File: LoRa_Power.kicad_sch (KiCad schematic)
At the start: 12 parts, among them U15 TPS7A4501DCQT, U16 ADM1176-1ARMZ-R7, U7 E22-900M30S

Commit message: temp
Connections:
- net LoRa_CSn is gone; now on net CSn: U7.19 (NSS)
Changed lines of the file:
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@@
+		)
+	)
+	(label "LoRa_CSn"
+		(at 243.84 123.19 0)
+		(fields_autoplaced yes)
+		(effects
+			(font
+				(size 1.27 1.27)
+			)
+			(justify left bottom)
 		)
 	)
@@
 	(label "CLK"
 		(at 243.84 127 0)
-		(fields_autoplaced yes)
-		(effects
-			(font
-				(size 1.27 1.27)
-			)
-			(justify left bottom)
-		)
-	)
-	(label "CSn"
-		(at 243.84 123.19 0)
 		(fields_autoplaced yes)
 		(effects
@@
 		)
 	)
-	(hierarchical_label "SDA_BUS"
+	(hierarchical_label "SDA"
 		(shape bidirectional)
 		(at 260.35 52.07 0)
@@
 		)
 	)
-	(hierarchical_label "SCL_BUS"
+	(hierarchical_label "SCL"
 		(shape bidirectional)
 		(at 260.35 49.53 0)

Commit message: v1 done
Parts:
- removed R53, R54: 10K, Resistor_SMD:R_0603_1608Metric, symbol Device:R_Small
- added R23, R24: 10K, Resistor_SMD:R_0603_1608Metric, symbol Device:R_Small
- U15: symbol Mainboard:TPS7A4501DCQT -> Argus-IC:TPS7A4501DCQT
- U16: symbol Mainboard:ADM1176-1ARMZ-R7 -> Argus-IC:ADM1176-1ARMZ-R7
- U7: symbol Mainboard:E22-900M30S -> Argus-Miscellaneous:E22-900M30S-SX1262
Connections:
- net GND: now also R23.2, R24.2
- net LoRa_RX_EN: now also R24.1
- net LoRa_TX_EN: now also R23.1

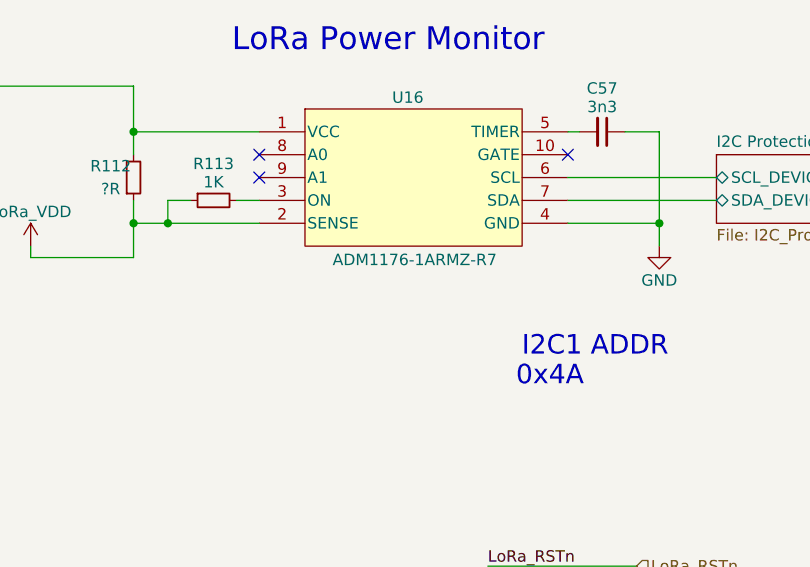
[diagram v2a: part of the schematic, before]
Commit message: Updated i2c device addresses and mcu caps
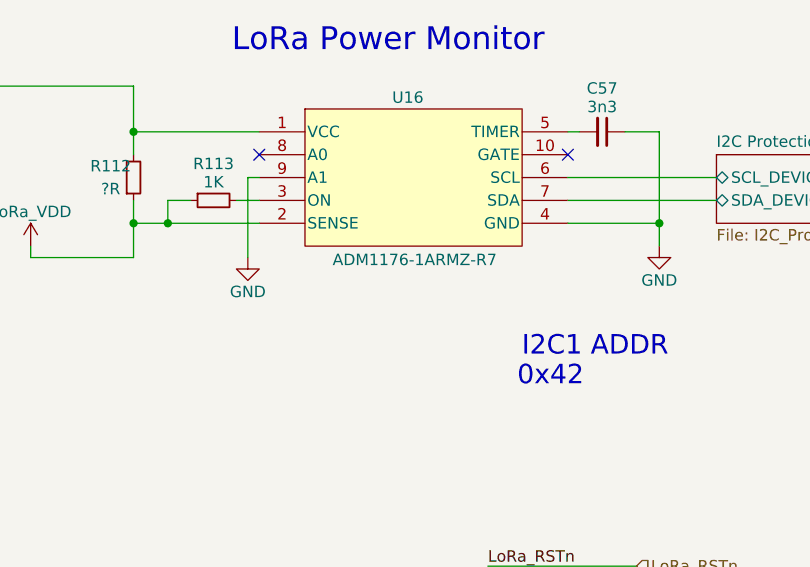
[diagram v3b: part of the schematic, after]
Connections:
- net GND: now also U16.9 (A1)
- no-connect marks 4 -> 3
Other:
- note added: "0x42"
- note removed: "0x4A"
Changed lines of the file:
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@@
 	)
 	(no_connect
-		(at 176.53 49.53)
+		(at 210.82 46.99)
 	)
 	(no_connect
 		(at 176.53 46.99)
 	)
-	(no_connect
-		(at 210.82 46.99)
-	)
 	(wire
 		(pts
@@
 	(wire
 		(pts
+			(xy 175.26 49.53) (xy 175.26 58.42)
+		)
+		(stroke
+			(width 0)
+			(type default)
+		)
+	)
+	(wire
+		(pts
 			(xy 39.37 143.51) (xy 39.37 140.97)
 		)
@@
 		(pts
 			(xy 106.68 52.07) (xy 106.68 59.69)
+		)
+		(stroke
+			(width 0)
+			(type default)
+		)
+	)
+	(wire
+		(pts
+			(xy 176.53 49.53) (xy 175.26 49.53)
 		)
 		(stroke
@@
 		)
 	)
-	(text "0x4A"
+	(text "0x42"
 		(exclude_from_sim no)
 		(at 212.598 72.898 0)
@@
 					(unit 1)
 				)
+			)
+		)
+	)
+	(symbol
+		(lib_id "power:GND")
+		(at 175.26 58.42 0)
+		(unit 1)
+		(exclude_from_sim no)
+		(in_bom yes)
+		(on_board yes)
+		(dnp no)
+		(property "Reference" "#PWR0154"
+			(at 175.26 64.77 0)
+			(effects
+				(font
+					(size 1.27 1.27)
+				)
+				(hide yes)
+			)
+		)
+		(property "Value" "GND"
+			(at 175.26 62.23 0)
+			(effects
+				(font
+					(size 1.27 1.27)
+				)
+			)
+		)
+		(property "Footprint" ""
+			(at 175.26 58.42 0)
+			(effects
+				(font
+					(size 1.27 1.27)
+				)
+				(hide yes)
+			)
+		)
+		(property "Datasheet" ""
+			(at 175.26 58.42 0)
+			(effects
+				(font
+					(size 1.27 1.27)
+				)
+				(hide yes)
+			)
+		)
+		(property "Description" "Power symbol creates a global label with name \"GND\" , ground"
+			(at 175.26 58.42 0)
+			(effects
+				(font
+					(size 1.27 1.27)
+				)
+				(hide yes)
+			)
+		)
+		(pin "1"
+		)
+		(instances
+			(project "Avionics-MainBoard"
+				(path "/4c932743-8c6f-426e-9c1f-5a3f2b32c70d/6167394f-ef17-4174-a137-33bfda5b3a14"
+					(reference "#PWR0154")
+					(unit 1)
+				)

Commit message: Added extra connector
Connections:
- net LoRa_DIO1: no longer U7.13 (DIO1)
- net LoRa_DIO2: no longer U7.8 (DIO2)
- no-connect marks 3 -> 5
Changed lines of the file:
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@@
+	)
+	(no_connect
+		(at 95.25 124.46)
 	)
 	(no_connect
@@
 		(at 176.53 46.99)
 	)
+	(no_connect
+		(at 60.96 134.62)
+	)
 	(wire
 		(pts
@@
 	(wire
 		(pts
-			(xy 95.25 124.46) (xy 110.49 124.46)
-		)
-		(stroke
-			(width 0)
-			(type default)
-		)
-	)
-	(wire
-		(pts
 			(xy 77.47 58.42) (xy 77.47 55.88)
 		)
@@
 		(pts
 			(xy 106.68 60.96) (xy 106.68 59.69)
-		)
-		(stroke
-			(width 0)
-			(type default)
-		)
-	)
-	(wire
-		(pts
-			(xy 49.53 134.62) (xy 60.96 134.62)
 		)
 		(stroke
@@
 		)
 	)
-	(label "LoRa_DIO1"
-		(at 99.06 124.46 0)
+	(label "LoRa_TX_EN"
+		(at 36.83 132.08 0)
 		(fields_autoplaced yes)
 		(effects
@@
 		)
 	)
-	(label "LoRa_TX_EN"
-		(at 36.83 132.08 0)
-		(fields_autoplaced yes)
-		(effects
-			(font
-				(size 1.27 1.27)
-			)
-			(justify left bottom)
-		)
-	)
 	(label "MISO"
 		(at 243.84 134.62 0)
 		(fields_autoplaced yes)
 		(effects
-			(font
-				(size 1.27 1.27)
-			)
-			(justify left bottom)
-		)
-	)
-	(label "LoRa_DIO2"
-		(at 49.53 134.62 0)
-		(fields_autoplaced yes)
-		(effects

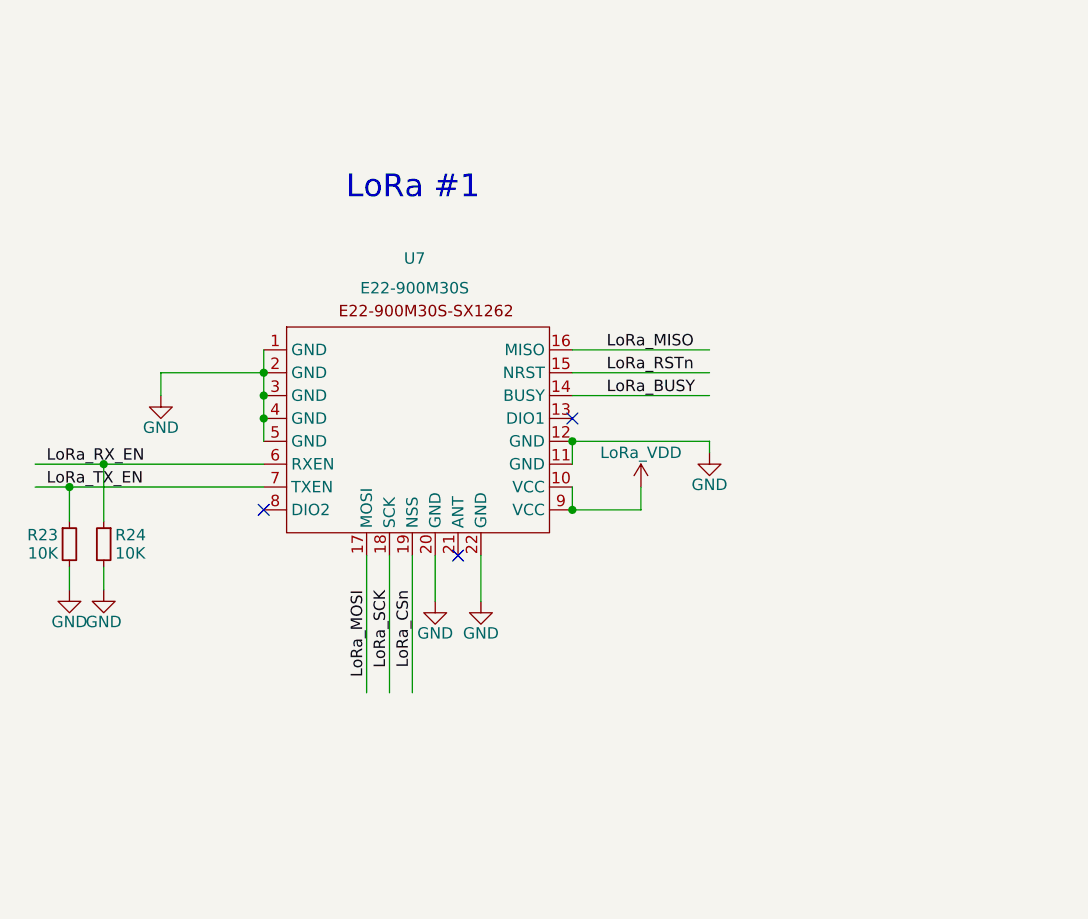
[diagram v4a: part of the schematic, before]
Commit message: Silkscreen hiding
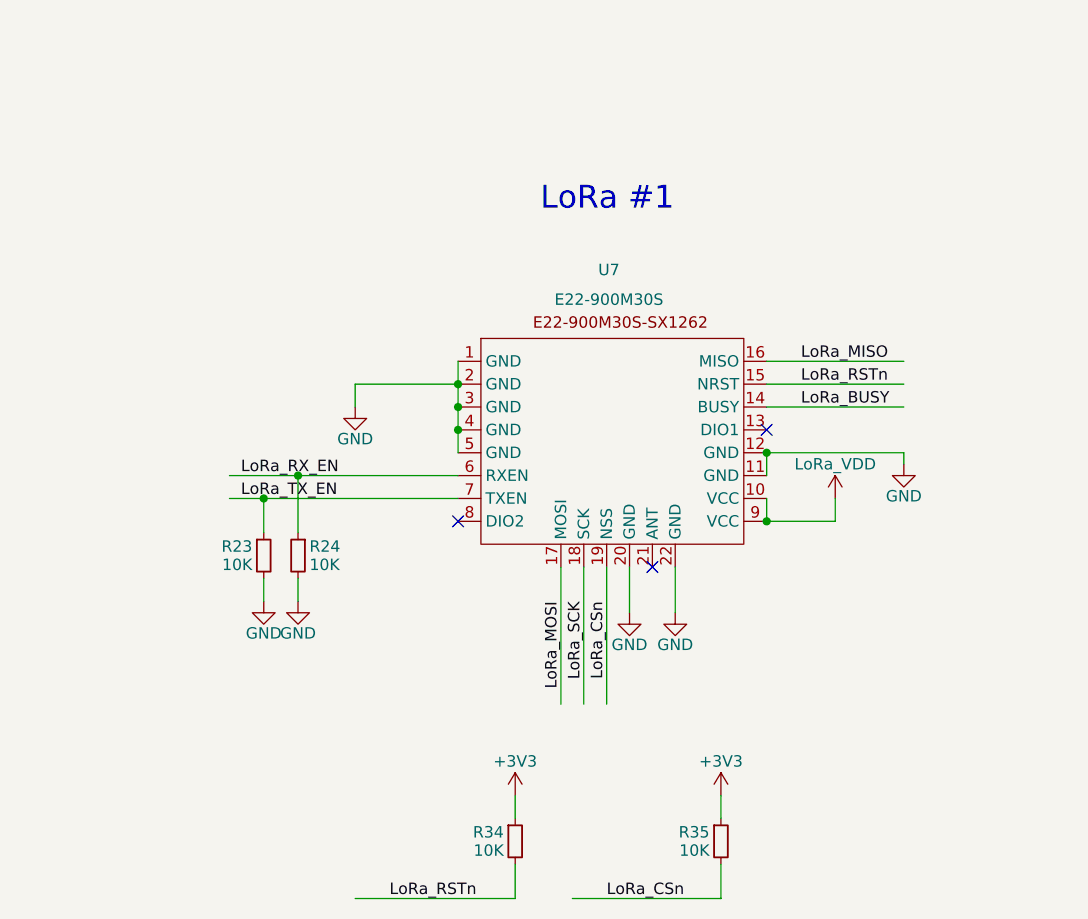
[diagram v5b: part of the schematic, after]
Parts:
- added R34, R35: 10K, Resistor_SMD:R_0603_1608Metric, symbol Device:R_Small
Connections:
- net CSn: now also R35.2
- net LoRa_RSTn: now also R34.2
- new net +3V3: R34.1, R35.1
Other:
- moved on the sheet: R23, R24, U7

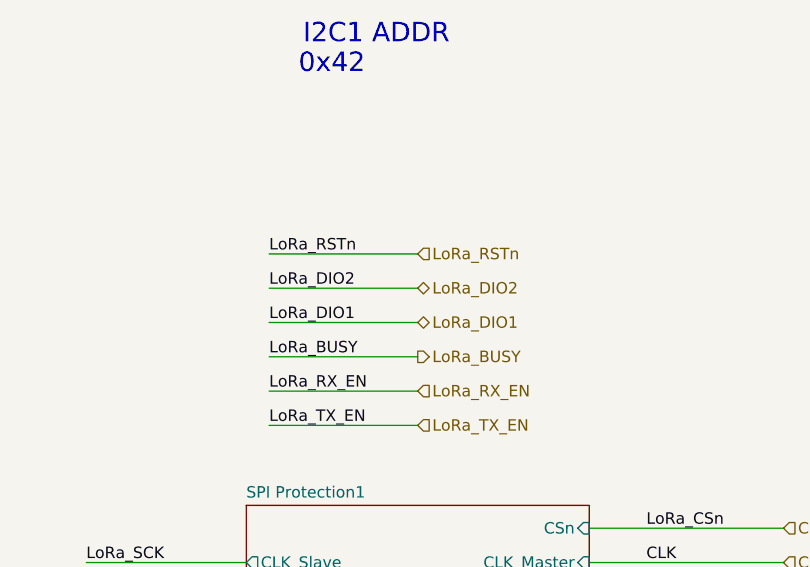
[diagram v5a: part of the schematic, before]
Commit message: Fixed schematic bugs and corresponding layout modifications
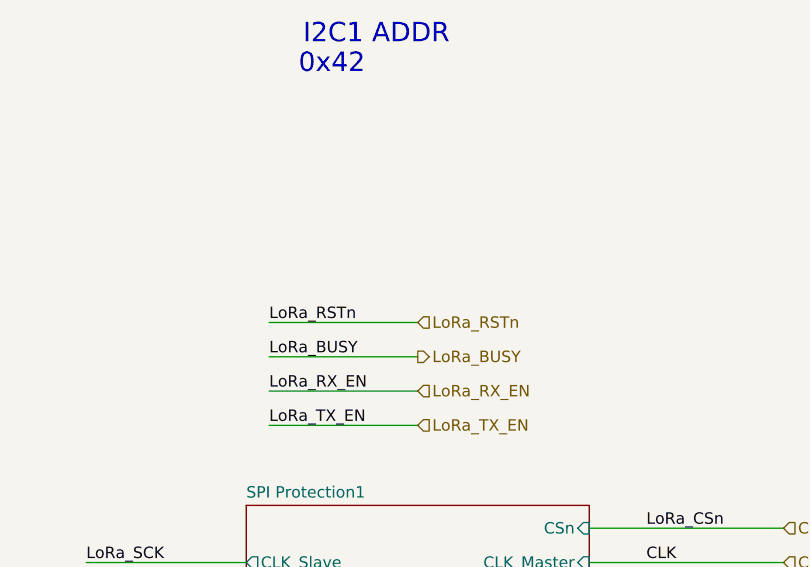
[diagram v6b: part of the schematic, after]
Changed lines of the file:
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@@
 	(wire
 		(pts
-			(xy 201.93 92.71) (xy 218.44 92.71)
+			(xy 201.93 100.33) (xy 218.44 100.33)
 		)
 		(stroke
@@
 	(wire
 		(pts
-			(xy 201.93 96.52) (xy 218.44 96.52)
-		)
-		(stroke
-			(width 0)
-			(type default)
-		)
-	)
-	(wire
-		(pts
 			(xy 111.76 173.99) (xy 111.76 177.8)
 		)
@@
 		(pts
 			(xy 82.55 123.19) (xy 82.55 125.73)
-		)
-		(stroke
-			(width 0)
-			(type default)
-		)
-	)
-	(wire
-		(pts
-			(xy 201.93 100.33) (xy 218.44 100.33)
 		)
 		(stroke
@@
 		)
 	)
-	(label "LoRa_DIO2"
-		(at 201.93 96.52 0)
-		(fields_autoplaced yes)
-		(effects
-			(font
-				(size 1.27 1.27)
-			)
-			(justify left bottom)
-		)
-	)
 	(label "LoRa_MOSI"
 		(at 181.61 130.81 0)
@@
 		)
 	)
-	(label "LoRa_DIO1"
-		(at 201.93 100.33 0)
-		(fields_autoplaced yes)
-		(effects
-			(font
-				(size 1.27 1.27)
-			)
-			(justify left bottom)
-		)
-	)
 	(label "LoRa_CSn"
 		(at 99.06 144.78 270)
@@
 	)
 	(label "LoRa_RSTn"
-		(at 201.93 92.71 0)
+		(at 201.93 100.33 0)
 		(fields_autoplaced yes)
 		(effects
@@
 			)
 			(justify left bottom)
-		)
-	)
-	(hierarchical_label "LoRa_DIO2"
-		(shape bidirectional)
-		(at 218.44 96.52 0)
-		(fields_autoplaced yes)
-		(effects
-			(font
-				(size 1.27 1.27)
-			)
-			(justify left)
 		)
 	)
@@
 	(hierarchical_label "LoRa_RSTn"
 		(shape input)
-		(at 218.44 92.71 0)
+		(at 218.44 100.33 0)
 		(fields_autoplaced yes)
 		(effects
@@
 		(fields_autoplaced yes)
 		(effects
-			(font
-				(size 1.27 1.27)
-			)
-			(justify left)
-		)
-	)
-	(hierarchical_label "LoRa_DIO1"
-		(shape bidirectional)
-		(at 218.44 100.33 0)
-		(fields_autoplaced yes)
-		(effects

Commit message: Minor fixes, export BOM
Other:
- moved on the sheet: C57
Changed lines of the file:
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@@
 	(wire
 		(pts
-			(xy 210.82 44.45) (xy 212.09 44.45)
+			(xy 210.82 44.45) (xy 213.36 44.45)
 		)
 		(stroke
@@
 	(wire
 		(pts
-			(xy 220.98 44.45) (xy 217.17 44.45)
+			(xy 220.98 44.45) (xy 218.44 44.45)
 		)
 		(stroke
@@
 		(dnp no)
 		(property "Reference" "R112"
-			(at 160.02 48.26 0)
+			(at 158.75 48.514 0)
 			(effects
 				(font
@@
 		)
 		(property "Value" "?R"
-			(at 160.02 50.8 0)
+			(at 160.02 50.546 0)
 			(effects
 				(font
@@
 	(symbol
 		(lib_id "Device:C_Small")
-		(at 214.63 44.45 270)
+		(at 215.9 44.45 270)
 		(unit 1)
 		(exclude_from_sim no)
@@
 		(dnp no)
 		(property "Reference" "C57"
-			(at 214.63 39.624 90)
+			(at 215.9 39.624 90)
 			(effects
 				(font
@@
 		)
 		(property "Value" "3n3"
-			(at 214.63 41.6814 90)
+			(at 215.9 41.6814 90)
 			(effects
 				(font
@@
 		)
 		(property "Footprint" "Capacitor_SMD:C_0603_1608Metric"
-			(at 214.63 44.45 0)
+			(at 215.9 44.45 0)
 			(effects
 				(font
@@
 		)
 		(property "Datasheet" ""
-			(at 214.63 44.45 0)
+			(at 215.9 44.45 0)
 			(effects
 				(font
@@
 		)
 		(property "Description" "3.3nF +-10% 100V X7R 0603"
-			(at 214.63 44.45 0)
-			(effects
-				(font
+			(at 215.9 44.45 0)
+			(effects
+				(font

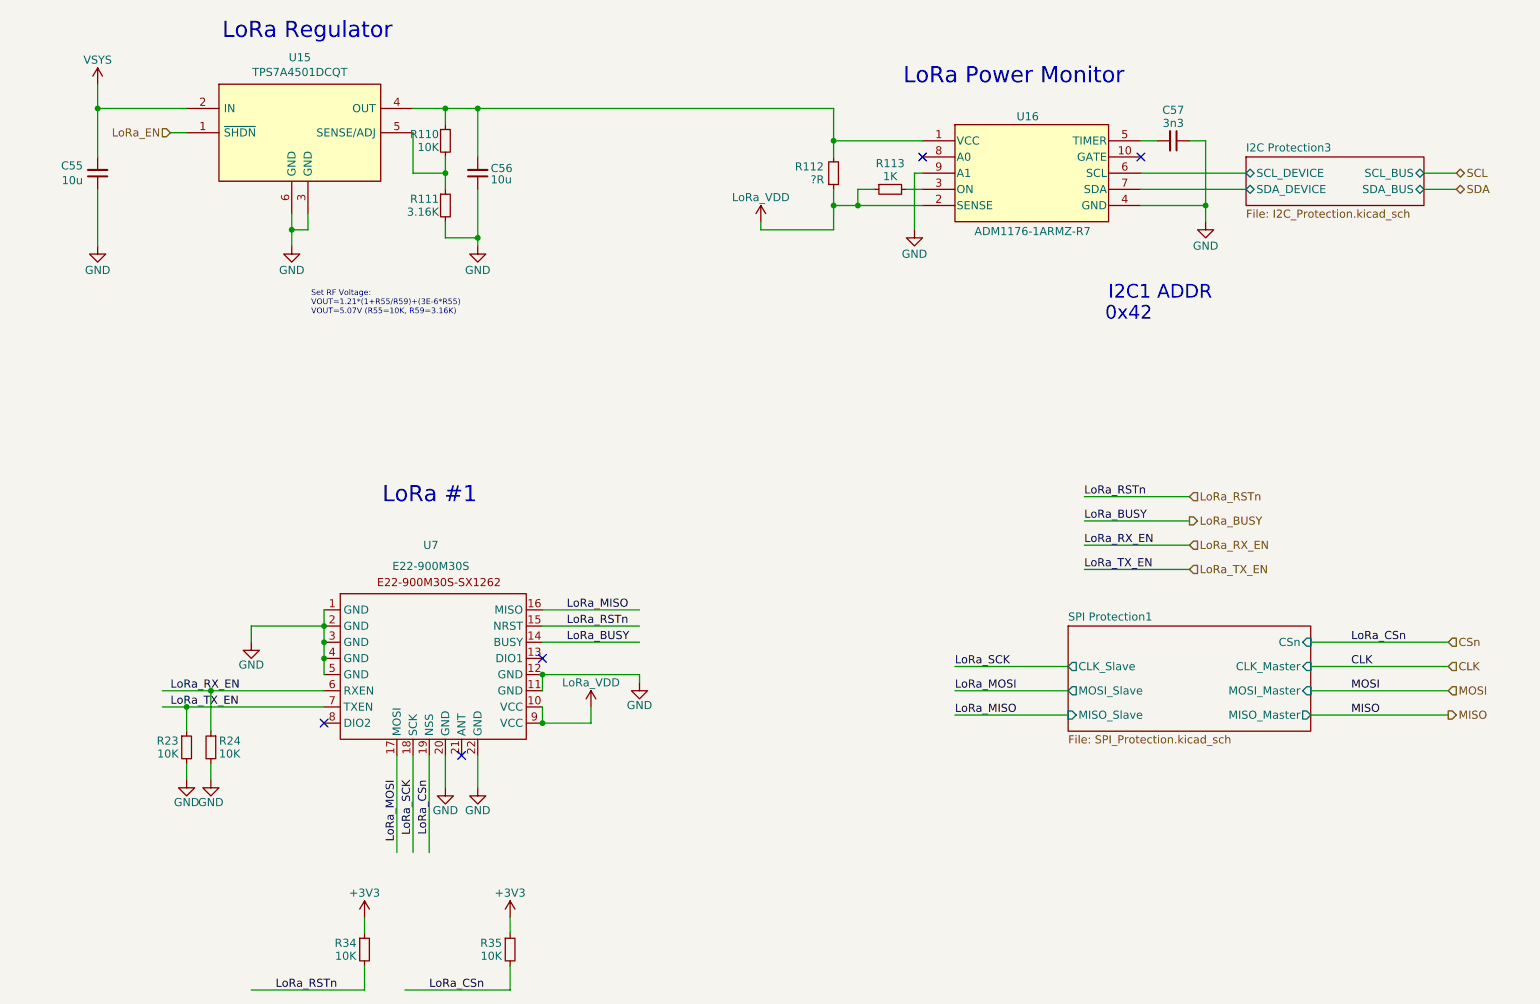
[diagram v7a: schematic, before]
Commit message: Added better protection to SD card, Jetson IO, and added address breakouts to power monitors
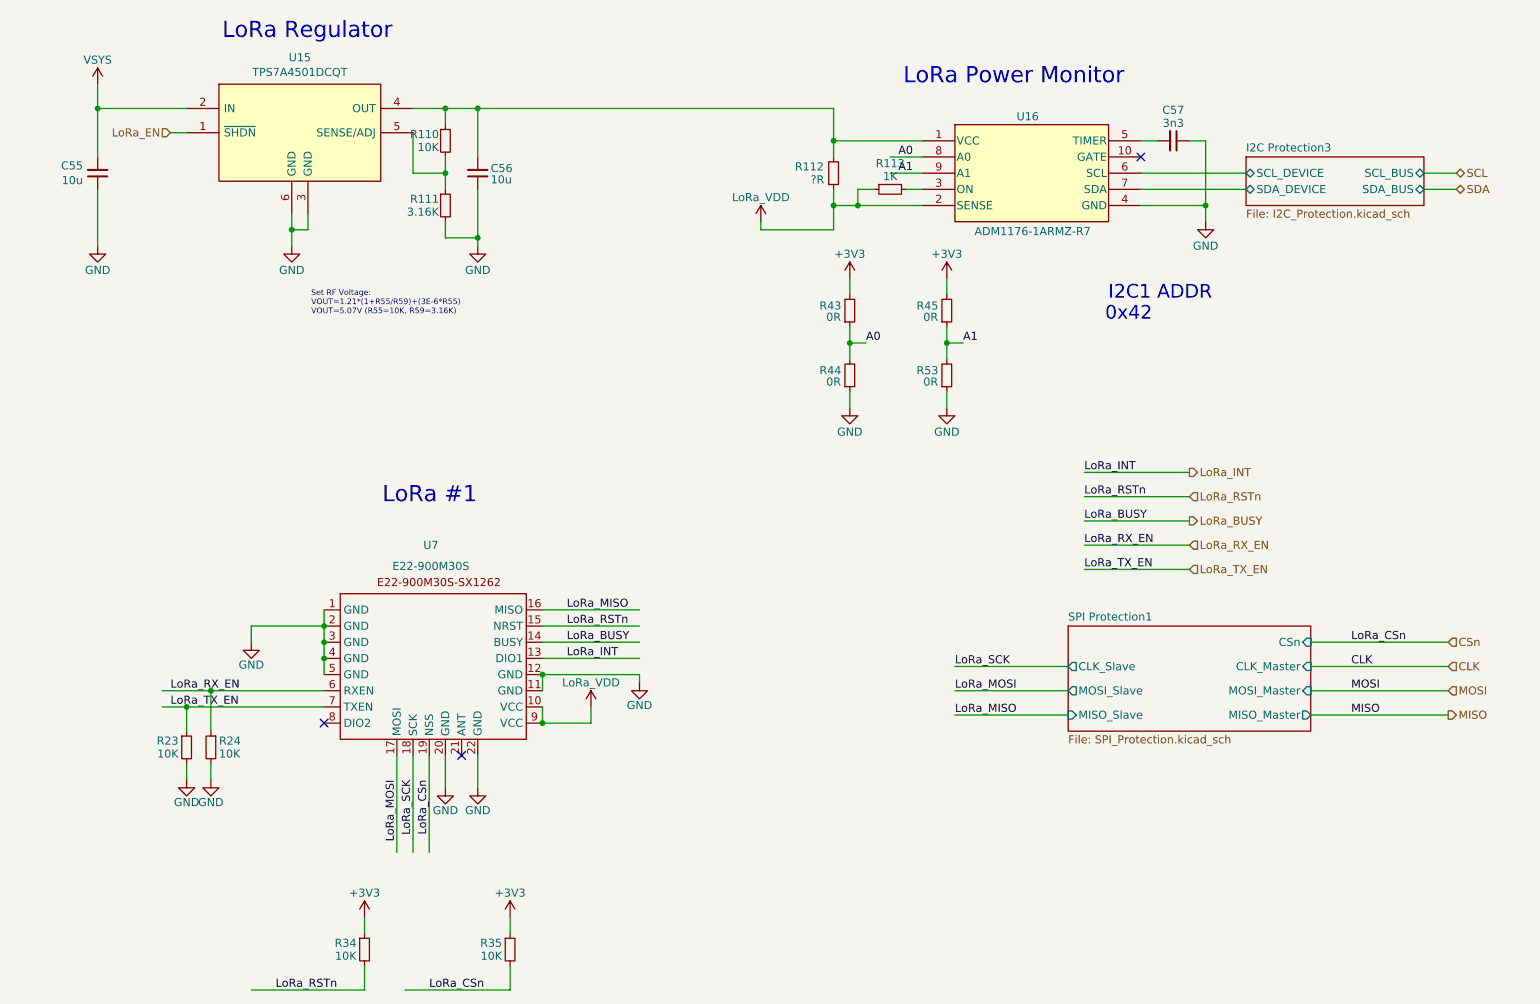
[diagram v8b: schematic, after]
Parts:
- added R43, R44, R45, R53: 0R, Resistor_SMD:R_0603_1608Metric, symbol Device:R_Small
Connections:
- net +3V3: now also R43.2, R45.2
- net GND: now also R44.1, R53.1; no longer U16.9 (A1)
- net LoRa_INT: now reaches U7.13 (DIO1)
- net A0: now reaches U16.8 (A0)
- net A0: now also R43.1, R44.2
- new net A1: R45.1, R53.2, U16.9 (A1)
- no-connect marks 5 -> 3
